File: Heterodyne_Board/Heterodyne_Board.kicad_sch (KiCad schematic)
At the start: 40 parts, among them J1 AVR-ISP-6, SW1 SW_SPST, U1 ATtiny85-20P, U2 TLV9054xD, U3 AP2112K-3.3, U4 LM386, U5 W25X40CLSN

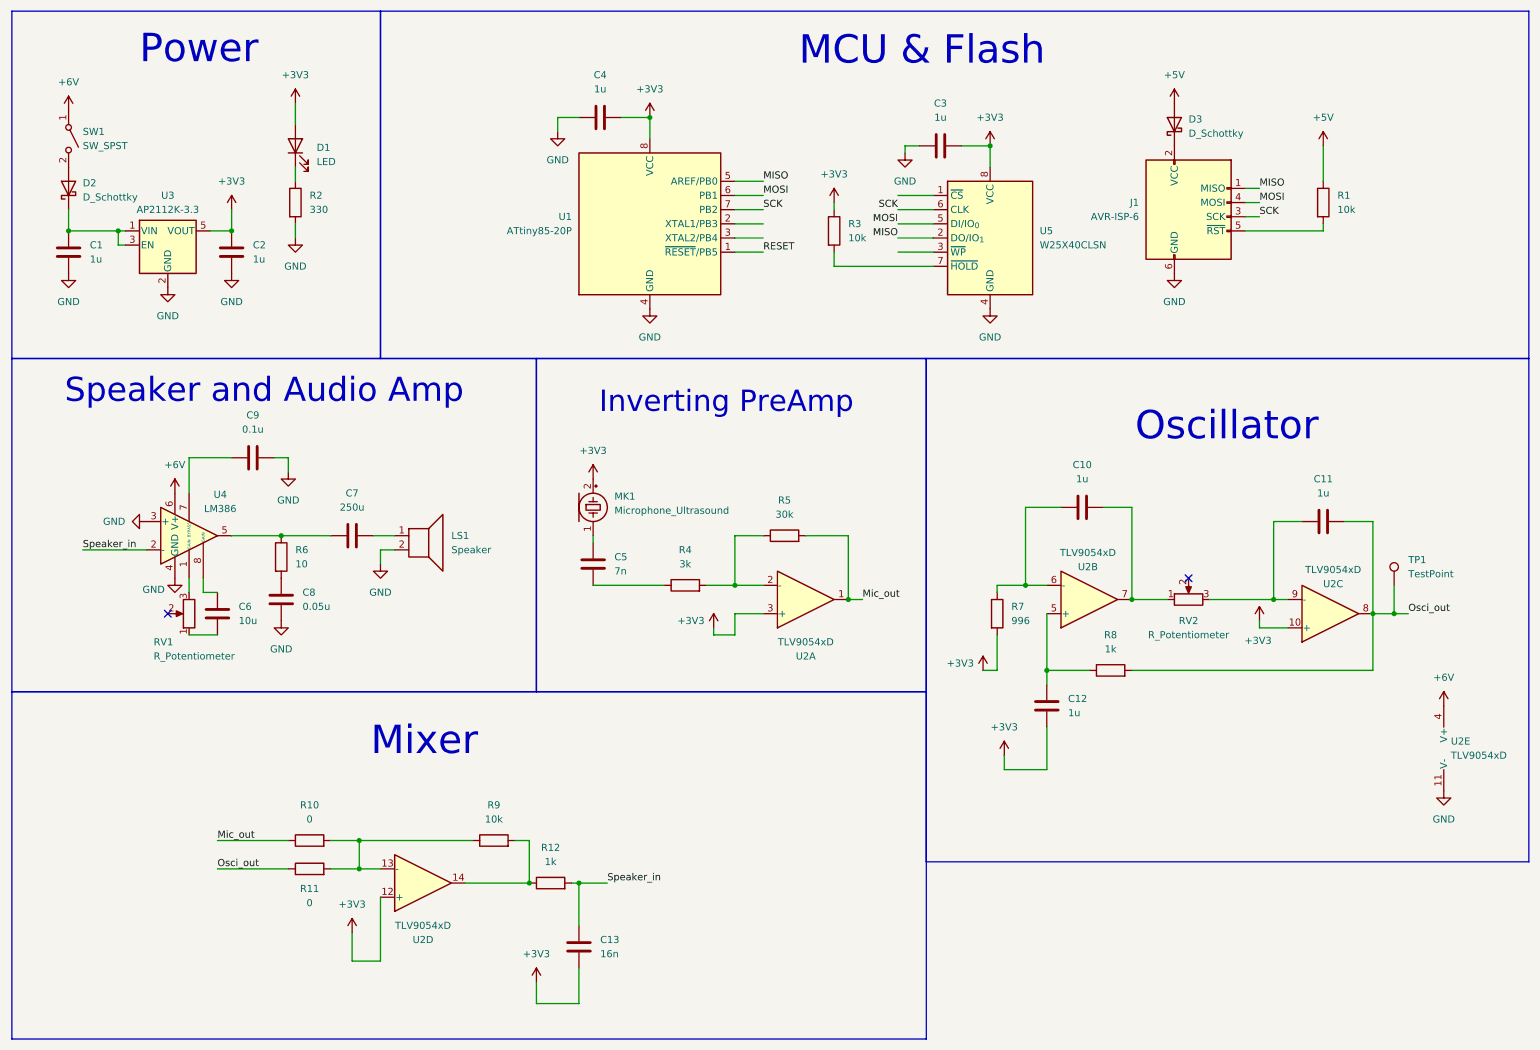
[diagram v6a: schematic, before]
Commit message: i brokje everything
got rid of the mixer bc i made an adder instead!!!! HECK!!!! audio module fixed, oscillator still bad :((
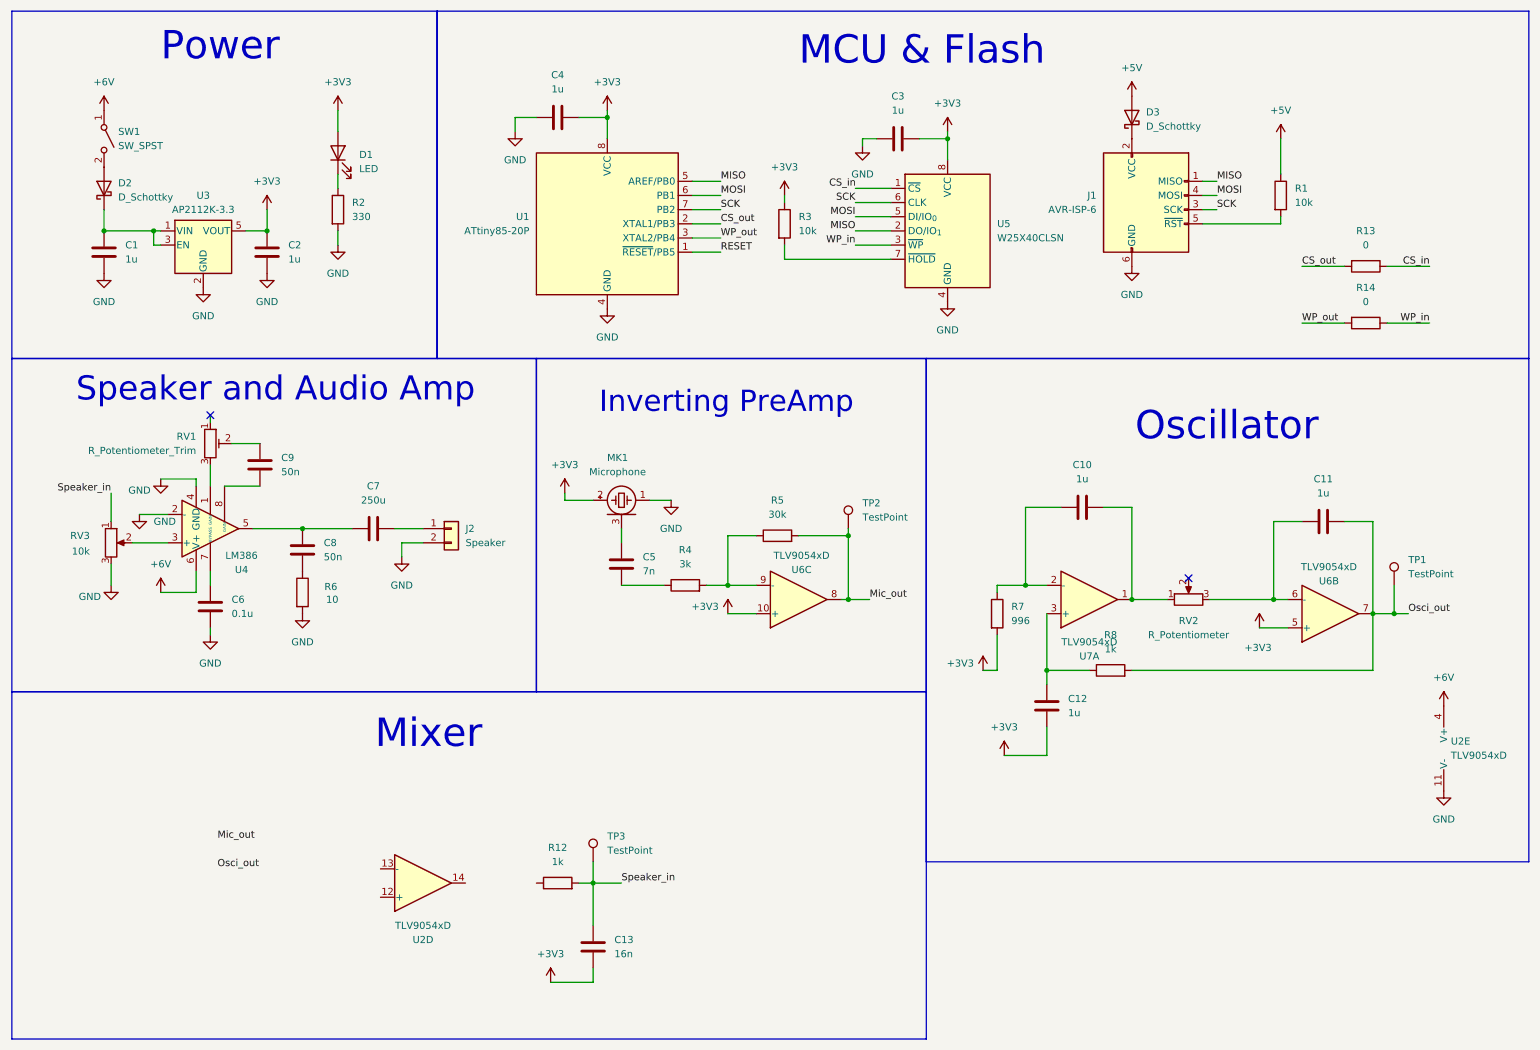
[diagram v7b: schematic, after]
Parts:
- removed LS1: Speaker, symbol Device:Speaker
- removed R10, R11: 0, symbol Device:R
- removed R9: 10k, symbol Device:R
- removed RV1: R_Potentiometer, symbol Device:R_Potentiometer
- removed unit 2 of U2
- removed unit 1 of U2
- removed unit 3 of U2
- added J2: Speaker, symbol Connector_Generic:Conn_01x02
- added R13, R14: 0, symbol Device:R
- added RV1: R_Potentiometer_Trim, symbol Device:R_Potentiometer_Trim
- added RV3: 10k, symbol Device:R_Potentiometer
- added TP2, TP3: TestPoint, symbol Connector:TestPoint
- added U6, U7: TLV9054xD, Package_SO:SOIC-14_3.9x8.7mm_P1.27mm, symbol Amplifier_Operational:TLV9054xD
- C6: value 10u -> 0.1u
- C8: value 0.05u -> 50n
- C9: value 0.1u -> 50n
- MK1: value Microphone_Ultrasound -> Microphone
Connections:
- net +3V3: now also U6.10 (+), U6.5 (+); no longer U2.12 (+)
- net GND: now also C6.1, MK1.1 (-), R6.2, U4.2 (-), J2.2 (Pin_2), RV3.3; no longer C8.1, C9.2, U4.3 (+)
- net Mic_out: now also TP2.1, U6.8
- net Osci_out: now also U6.7
- net Speaker_in: now also RV3.1, TP3.1; no longer U4.2 (-)
- net at C10.2, RV2.1: now also U7.1
- net at C11.1, RV2.3: now also U6.6 (-)
- net at C12.1, R8.1: now also U7.3 (+)
- net at C10.1, R7.1: now also U7.2 (-)
- net at R12.1: no longer U2.14
- net at C7.2: now also J2.1 (Pin_1)
- net at C6.2: now also U4.7 (BYPASS)
- net at U4.1 (GAIN): now also RV1.3
- net CS_out: now reaches U1.2 (XTAL1/PB3)
- net CS_out: now also R13.2
- net WP_out: now reaches U1.3 (XTAL2/PB4)
- net WP_out: now also R14.2
- net at C9.1: now also U4.8 (GAIN); no longer U4.7 (BYPASS)
- net at C8.2: now also C7.1, U4.5; no longer R6.2
- net at C5.1: now also MK1.3 (+); no longer MK1.1 (-)
- net CS_in: now reaches U5.1 (~{CS})
- net CS_in: now also R13.1
- net WP_in: now reaches U5.3 (~{WP})
- net WP_in: now also R14.1
- net at R4.2, R5.1: now also U6.9 (-)
- new net: C8.1, R6.1
- new net: C9.2, RV1.2
- new net: RV3.2, U4.3 (+)
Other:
- moved on the sheet: C1, C13, C2, C3, C4, C5, C7, C8, D1, D2, D3, J1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

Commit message: fixed osc and mixer
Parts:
- removed C12: 1u, symbol Device:C
- removed C13: 16n, symbol Device:C
- removed RV2: R_Potentiometer, symbol Device:R_Potentiometer
- removed TP1, TP3: TestPoint, symbol Connector:TestPoint
- added C14: 1u, symbol Device:C
- added D4: D_Schottky, symbol Device:D_Schottky
- added R10, R11, R9: 1k, symbol Device:R
- added R15: 470, symbol Device:R
- added R16: 10k, symbol Device:R
- added RV4: R_Potentiometer, symbol Device:R_Potentiometer
- C10: value 1u -> 22n
- C11: value 1u -> 4.7n
- R7: value 996 -> 1k
- R8: value 1k -> 100
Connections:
- net +3V3: now also C10.1, C11.1, R7.1, U2.12 (+), C14.2, D4.1 (K); no longer R7.2, U6.5 (+)
- net Mic_out: now also R9.1
- net Osci_out: now also R12.2, R8.1, U7.1, R10.1; no longer C11.2, R8.2, U6.7
- net Speaker_in: now also U2.14, R16.2; no longer R12.2
- net at C10.2: now also C11.2, U7.2 (-), RV4.1; no longer U7.1
- net at U6.6 (-): no longer C11.1
- net at R12.1: now also R7.2, U7.3 (+)
- net at U2.13 (-): now also R15.2, R16.1
- new net: D4.2 (A), R10.2, R11.1, R9.2
- new net: R8.2, RV4.3
- new net: C14.1, R11.2, R15.1
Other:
- moved on the sheet: U2D, U6B
